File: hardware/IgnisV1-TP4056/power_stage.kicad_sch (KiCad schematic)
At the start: 39 parts, among them J1 530480210, J2 RCV_Coil, Q1 DMP1045U, U1 TP4056-42-ESOP8, U2 FP6277XR-G1, U4 BQ51013BRHLT

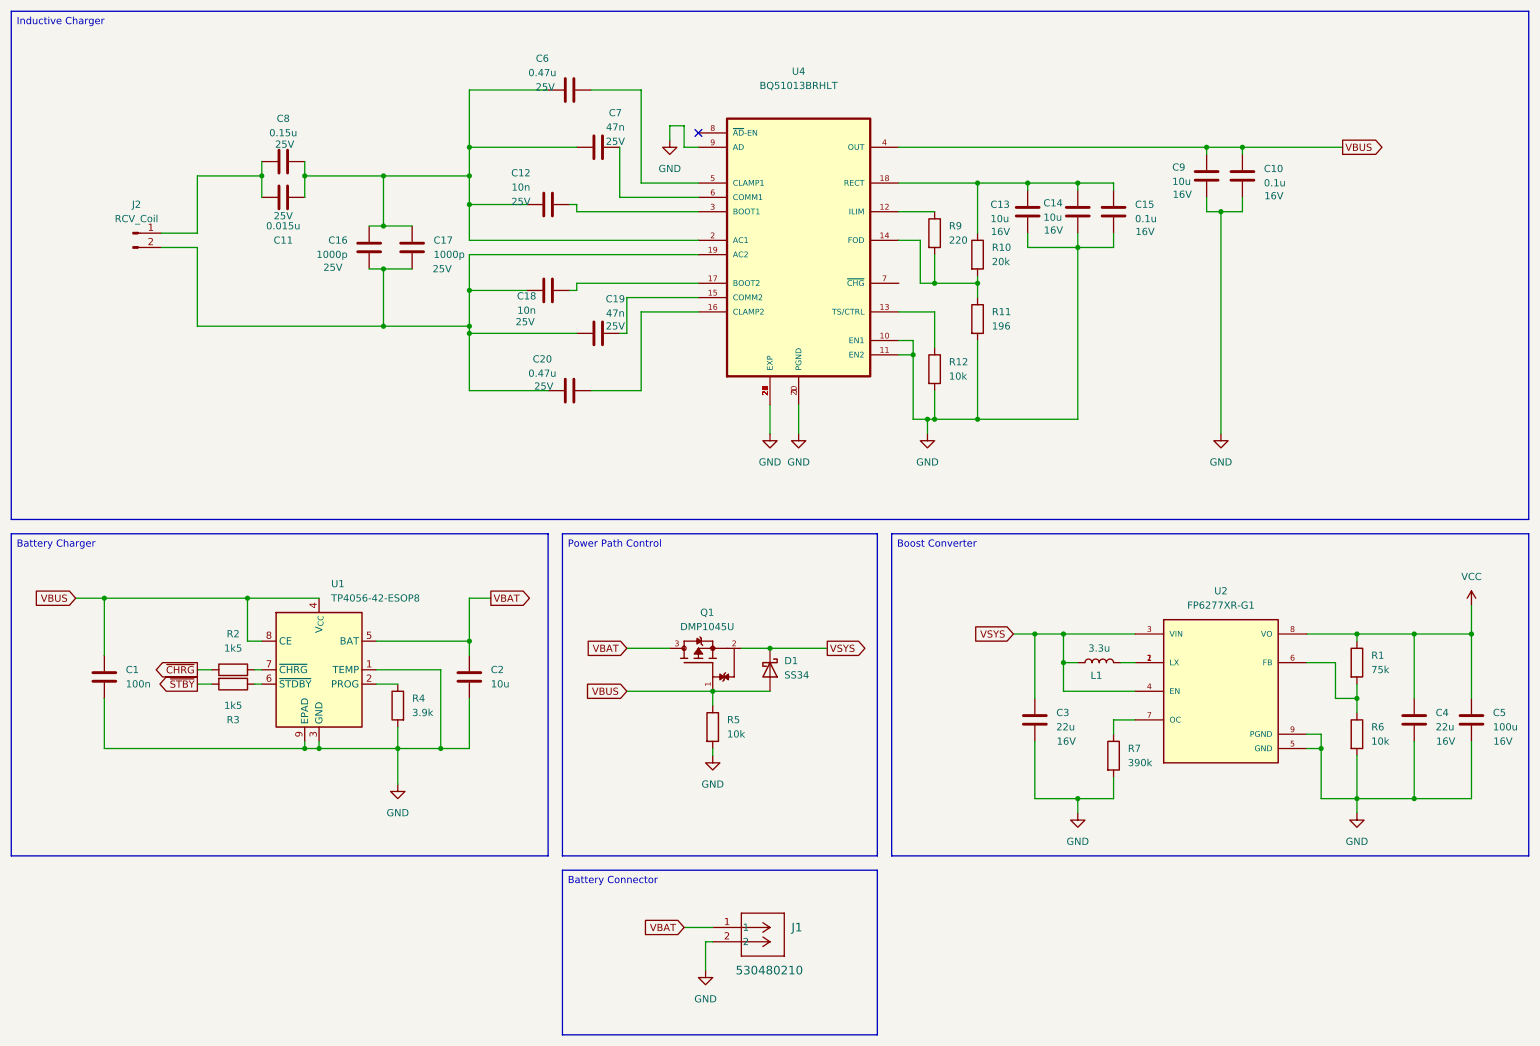
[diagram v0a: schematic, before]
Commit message: ⚡ Rework LED strip and add shock switch filtering
Includes rework of the LED strip
Includes filter with schmidt trigger buffer to input shock switch SW18030
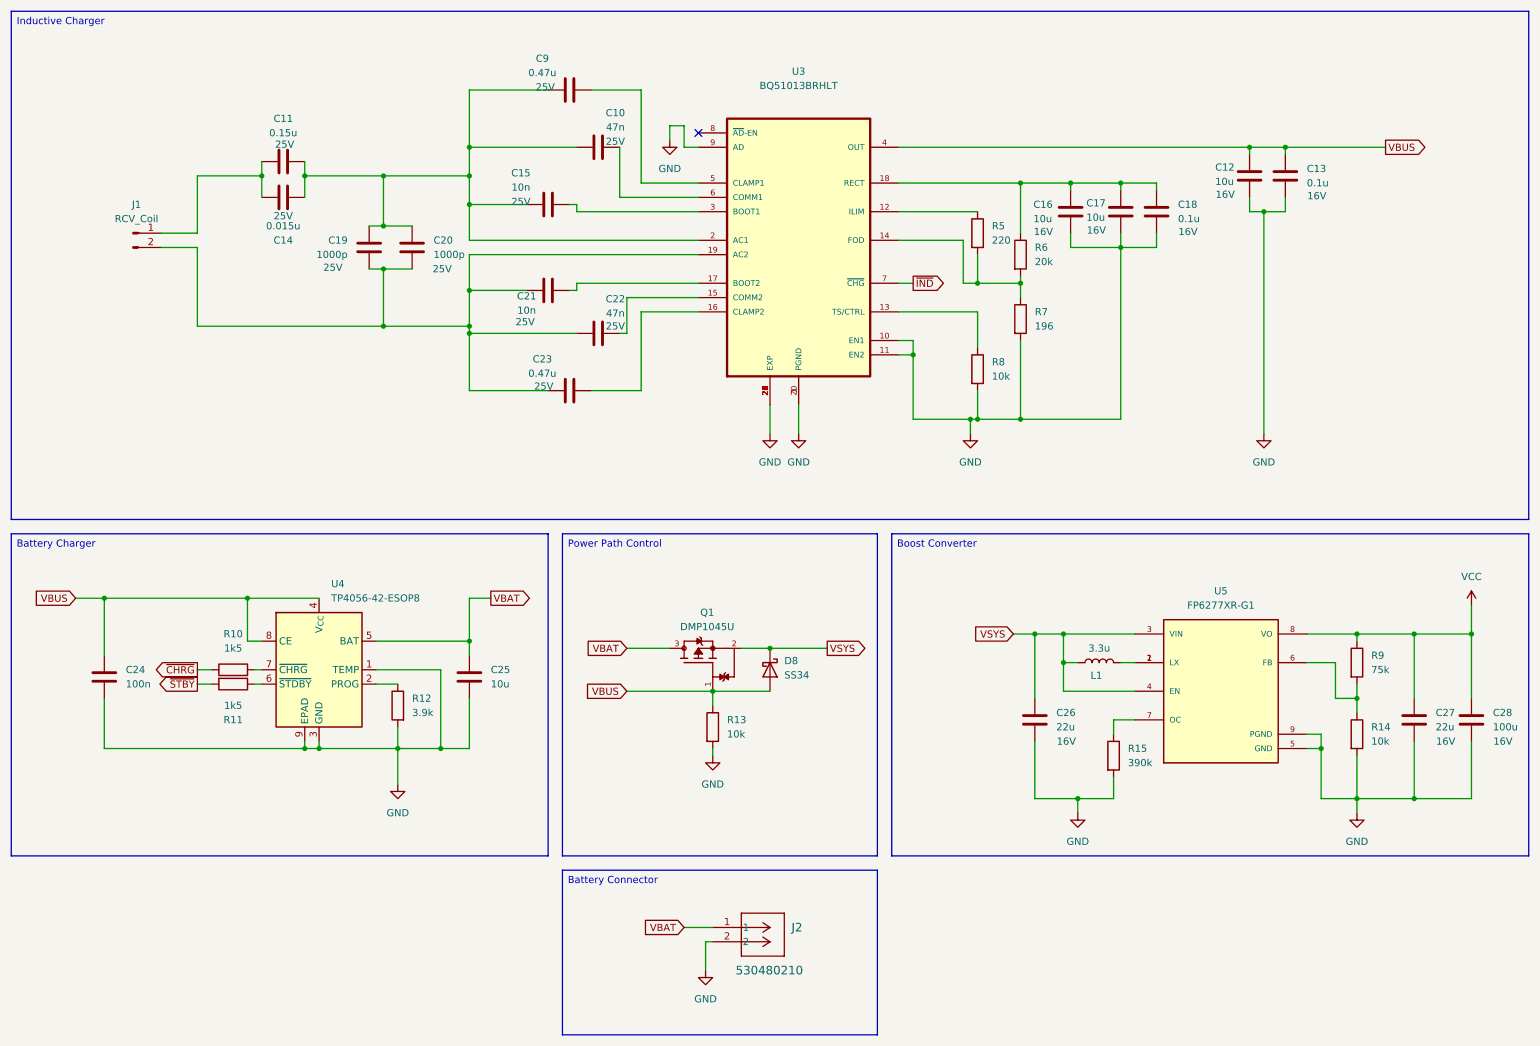
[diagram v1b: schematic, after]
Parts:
- renumbered C7 to C10, C8 to C11, C9 to C12, C10 to C13, C11 to C14, C12 to C15, C13 to C16, C14 to C17, C15 to C18, C16 to C19, C17 to C20, C18 to C21, C19 to C22, C20 to C23, C1 to C24, C2 to C25, C3 to C26, C4 to C27, C5 to C28, C6 to C9, D1 to D8, J2 to J1, J1 to J2, R2 to R10, R3 to R11, R4 to R12, R5 to R13, R6 to R14, R7 to R15, R9 to R5, R10 to R6, R11 to R7, R12 to R8, R1 to R9, U4 to U3, U1 to U4, U2 to U5
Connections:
- net ~{IND}: now reaches U3.7 (~{CHG})
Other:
- moved on the sheet: C12, C13, C16, C17, C18, R5, R6, R7, R8

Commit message: 🧩 Finalize IgnisV1-TP4056 schematics & add reference design
- Finished schematics by adding necessary pull-ups on signal lines.
- Copied electrical design from an older version for reference and traceability.
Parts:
- added R10: 220, symbol Device:R
- R14: renamed from R10; value 1k5 -> 220
- R15: renamed from R11; value 1k5 -> 220
- renumbered R7 to R11, R8 to R12, R9 to R13, R12 to R16, R13 to R17, R14 to R18, R15 to R19, R5 to R8, R6 to R9
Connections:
- net ~{IND}: now also R10.2; no longer U3.7 (~{CHG})
- new net: R10.1, U3.7 (~{CHG})
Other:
- moved on the sheet: C12, C13, C16, C17, C18, R11, R12, R8, R9

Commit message: 🎨 Complete logo cleanup and rebranding with new typography
- Changed official logo font from Museo Rounded to "Dongle" Bold
- Reorganized logo assets with consistent naming convention
- Added Makefile for automated PNG export in multiple variants and sizes
- Updated KiCAD worksheets for both IgnisV1 and IgnisV2 PCBs with new branding
- Removed obsolete logo files and consolidated SVG sources
- Exported updated schematic PDFs with refreshed corporate identity
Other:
- title: (none) -> Ignis
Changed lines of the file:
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@@
 	(generator_version "9.0")
 	(paper "A4")
+	(title_block
+		(title "Ignis")
+		(date "2025-08-24")
+		(rev "v1.1")
+	)
 	(text_box "Battery Connector"
 		(exclude_from_sim no)
